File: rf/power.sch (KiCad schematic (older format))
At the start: 23 parts

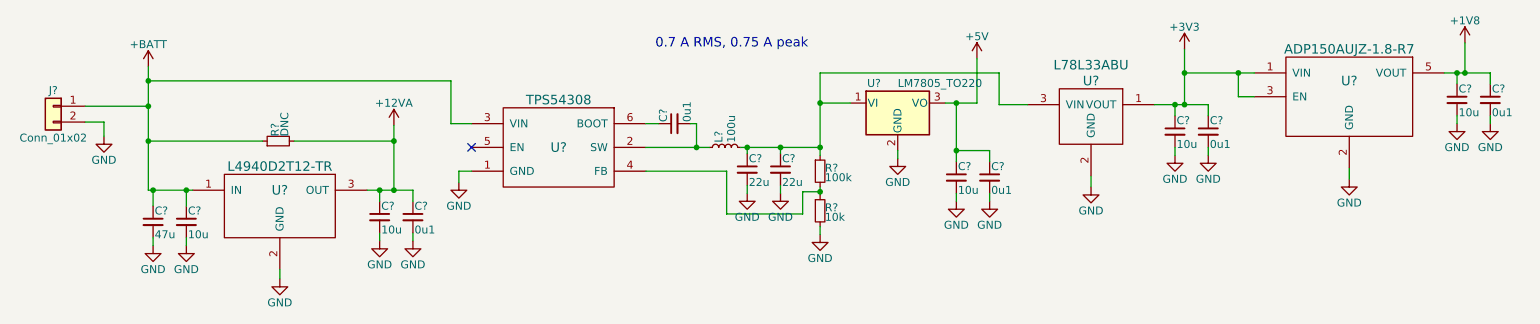
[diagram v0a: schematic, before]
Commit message: Finish assigning component footprints
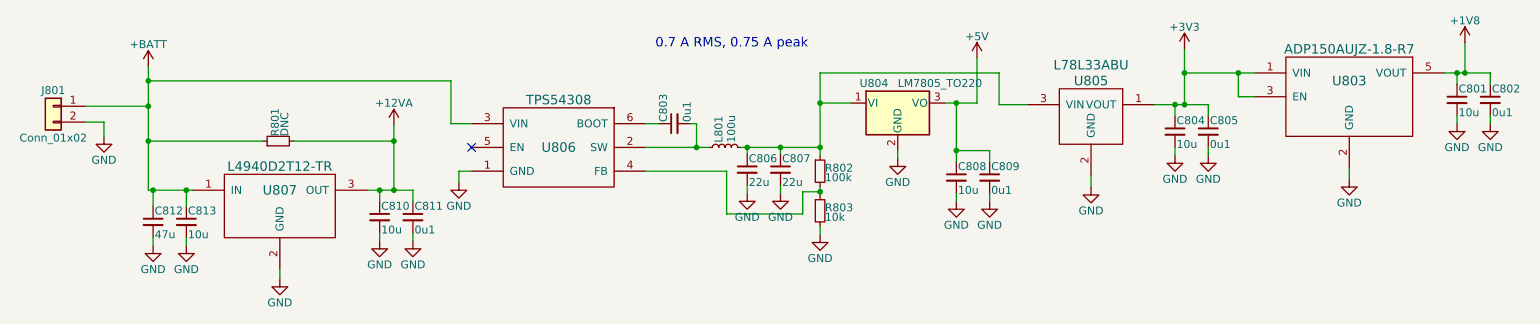
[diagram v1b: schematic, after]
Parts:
- gave numbers to parts that had none: 23

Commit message: Finish first revision layout
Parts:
- removed R801: DNC, Resistors_SMD:R_1206_HandSoldering, symbol R_Small
- removed U804: LM7805_TO220, TO_SOT_Packages_THT:TO-220_Vertical, symbol LM7805_TO220
- removed U807: L4940D2T12-TR, rajsradar:D2PAK, symbol L4940D2T12-TR
- added U802: LM340MPX-5.0/NOPB, TO_SOT_Packages_SMD:SOT-223-3_TabPin2, symbol LM340MPX-5.0/NOPB
- renumbered U803 to U801, U805 to U803, U806 to U804
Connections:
- net +BATT is gone; now on net +12VA: C812.1, C813.1, J801.1 (Pin_1), U804.3 (VIN)
- net +5V: now also U802.3 (VO)
- net GND: now also U802.2 (GND)
- net at C806.1, C807.1, L801.2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: now also U802.1 (VI)
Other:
- moved on the sheet: C810, C811
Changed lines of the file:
@@
 LIBS:mc2016k30
 LIBS:cp0402q5425entr
+LIBS:lm340-5
 EELAYER 25 0
 EELAYER END
@@
 L +12VA #PWR807
 U 1 1 5A9D8F76
-P 3295 3275
-F 0 "#PWR807" H 3295 3125 50  0001 C CNN
-F 1 "+12VA" H 3295 3415 50  0000 C CNN
-F 2 "" H 3295 3275 50  0001 C CNN
-F 3 "" H 3295 3275 50  0001 C CNN
-	1    3295 3275
+P 2305 3275
+F 0 "#PWR807" H 2305 3125 50  0001 C CNN
+F 1 "+12VA" H 2305 3415 50  0000 C CNN
+F 2 "" H 2305 3275 50  0001 C CNN
+F 3 "" H 2305 3275 50  0001 C CNN
+	1    2305 3275
 	1    0    0    -1
 $EndComp
@@
 $EndComp
 $Comp
-L R_Small R801
-U 1 1 5A9D8F94
-P 2565 3375
-F 0 "R801" H 2595 3395 50  0000 L CNN
-F 1 "DNC" H 2595 3335 50  0000 L CNN
-F 2 "Resistors_SMD:R_1206_HandSoldering" H 2565 3375 50  0001 C CNN
-F 3 "" H 2565 3375 50  0001 C CNN
-	1    2565 3375
-	0    -1   -1   0
-$EndComp
-$Comp
-L L4940D2T12-TR U807
-U 1 1 5A9D8F9B
-P 2575 3685
-F 0 "U807" H 2575 3685 60  0000 C CNN
-F 1 "L4940D2T12-TR" H 2575 3835 60  0000 C CNN
-F 2 "rajsradar:D2PAK" H 2575 3685 60  0001 C CNN
-F 3 "" H 2575 3685 60  0001 C CNN
-	1    2575 3685
-	1    0    0    -1
-$EndComp
-$Comp
-L TPS54308 U806
+L TPS54308 U804
 U 1 1 5A9D8FA2
 P 4335 3415
-F 0 "U806" H 4335 3415 60  0000 C CNN
+F 0 "U804" H 4335 3415 60  0000 C CNN
 F 1 "TPS54308" H 4335 3715 60  0000 C CNN
 F 2 "rajsradar:TI-SOT-23-6" H 4335 3415 60  0001 C CNN
@@
 NoConn ~ 3785 3415
 $Comp
-L GND #PWR824
-U 1 1 5A9D8FAA
-P 2575 4245
-F 0 "#PWR824" H 2575 3995 50  0001 C CNN
-F 1 "GND" H 2575 4095 50  0000 C CNN
-F 2 "" H 2575 4245 50  0001 C CNN
-F 3 "" H 2575 4245 50  0001 C CNN
-	1    2575 4245
-	1    0    0    -1
-$EndComp
-$Comp
-L GND #PWR813
+L GND #PWR812
 U 1 1 5A9D8FB0
 P 3705 3635
-F 0 "#PWR813" H 3705 3385 50  0001 C CNN
+F 0 "#PWR812" H 3705 3385 50  0001 C CNN
 F 1 "GND" H 3705 3485 50  0000 C CNN
 F 2 "" H 3705 3635 50  0001 C CNN
@@
 L C_Small C810
 U 1 1 5A9D8FF2
-P 3205 3855
-F 0 "C810" H 3215 3925 50  0000 L CNN
-F 1 "10u" H 3215 3775 50  0000 L CNN
-F 2 "Capacitors_SMD:C_0805_HandSoldering" H 3205 3855 50  0001 C CNN
-F 3 "" H 3205 3855 50  0001 C CNN
-	1    3205 3855
+P 2215 3855
+F 0 "C810" H 2225 3925 50  0000 L CNN
+F 1 "10u" H 2225 3775 50  0000 L CNN
+F 2 "Capacitors_SMD:C_0805_HandSoldering" H 2215 3855 50  0001 C CNN
+F 3 "" H 2215 3855 50  0001 C CNN
+	1    2215 3855
 	1    0    0    -1
 $EndComp
@@
 L C_Small C811
 U 1 1 5A9D8FF9
-P 3415 3855
-F 0 "C811" H 3425 3925 50  0000 L CNN
-F 1 "0u1" H 3425 3775 50  0000 L CNN
-F 2 "Capacitors_SMD:C_0603_HandSoldering" H 3415 3855 50  0001 C CNN
-F 3 "" H 3415 3855 50  0001 C CNN
-	1    3415 3855
+P 2425 3855
+F 0 "C811" H 2435 3925 50  0000 L CNN
+F 1 "0u1" H 2435 3775 50  0000 L CNN
+F 2 "Capacitors_SMD:C_0603_HandSoldering" H 2425 3855 50  0001 C CNN
+F 3 "" H 2425 3855 50  0001 C CNN
+	1    2425 3855
 	1    0    0    -1
 $EndComp
@@
 L GND #PWR820
 U 1 1 5A9D9000
-P 3205 4005
-F 0 "#PWR820" H 3205 3755 50  0001 C CNN
-F 1 "GND" H 3205 3855 50  0000 C CNN
-F 2 "" H 3205 4005 50  0001 C CNN
-F 3 "" H 3205 4005 50  0001 C CNN
-	1    3205 4005
+P 2215 4005
+F 0 "#PWR820" H 2215 3755 50  0001 C CNN
+F 1 "GND" H 2215 3855 50  0000 C CNN
+F 2 "" H 2215 4005 50  0001 C CNN
+F 3 "" H 2215 4005 50  0001 C CNN
+	1    2215 4005
 	1    0    0    -1
 $EndComp
@@
 L GND #PWR821
 U 1 1 5A9D9006
-P 3415 4005
-F 0 "#PWR821" H 3415 3755 50  0001 C CNN
-F 1 "GND" H 3415 3855 50  0000 C CNN
-F 2 "" H 3415 4005 50  0001 C CNN
-F 3 "" H 3415 4005 50  0001 C CNN
-	1    3415 4005
+P 2425 4005
+F 0 "#PWR821" H 2425 3755 50  0001 C CNN
+F 1 "GND" H 2425 3855 50  0000 C CNN
+F 2 "" H 2425 4005 50  0001 C CNN
+F 3 "" H 2425 4005 50  0001 C CNN
+	1    2425 4005
 	1    0    0    -1
 $EndComp
@@
 $EndComp
 $Comp
-L LM7805_TO220 U804
-U 1 1 5A9D9026
-P 6475 3135
-F 0 "U804" H 6325 3260 50  0000 C CNN
-F 1 "LM7805_TO220" H 6475 3260 50  0000 L CNN
-F 2 "TO_SOT_Packages_THT:TO-220_Vertical" H 6475 3360 50  0001 C CIN
-F 3 "" H 6475 3085 50  0001 C CNN
-	1    6475 3135
-	1    0    0    -1
-$EndComp
-$Comp
-L L78L33ABU U805
+L L78L33ABU U803
 U 1 1 5A9D902D
 P 7695 3145
-F 0 "U805" H 7695 3295 60  0000 C CNN
+F 0 "U803" H 7695 3295 60  0000 C CNN
 F 1 "L78L33ABU" H 7695 3395 60  0000 C CNN
 F 2 "TO_SOT_Packages_SMD:SOT-89-3_Handsoldering" H 7695 3145 60  0001 C CNN
@@
 $EndComp
 $Comp
-L ADP150AUJZ-1.8-R7 U803
+L ADP150AUJZ-1.8-R7 U801
 U 1 1 5A9D9034
 P 9325 2995
-F 0 "U803" H 9325 2995 60  0000 C CNN
+F 0 "U801" H 9325 2995 60  0000 C CNN
 F 1 "ADP150AUJZ-1.8-R7" H 9325 3195 60  0000 C CNN
 F 2 "rajsradar:TSOT-23" H 9325 2995 60  0001 C CNN
@@
 $EndComp
 $Comp
-L GND #PWR811
+L GND #PWR813
 U 1 1 5A9D903B
-P 6475 3485
-F 0 "#PWR811" H 6475 3235 50  0001 C CNN
-F 1 "GND" H 6475 3335 50  0000 C CNN
-F 2 "" H 6475 3485 50  0001 C CNN
-F 3 "" H 6475 3485 50  0001 C CNN
-	1    6475 3485
+P 6475 3650
+F 0 "#PWR813" H 6475 3400 50  0001 C CNN
+F 1 "GND" H 6475 3500 50  0000 C CNN
+F 2 "" H 6475 3650 50  0001 C CNN
+F 3 "" H 6475 3650 50  0001 C CNN
+	1    6475 3650
 	1    0    0    -1
 $EndComp
@@
 $EndComp
 $Comp
-L GND #PWR812
+L GND #PWR811
 U 1 1 5A9D9047
 P 9325 3615
-F 0 "#PWR812" H 9325 3365 50  0001 C CNN
+F 0 "#PWR811" H 9325 3365 50  0001 C CNN
 F 1 "GND" H 9325 3465 50  0000 C CNN
 F 2 "" H 9325 3615 50  0001 C CNN
@@
 	1745 2905 1745 3685
 Wire Wire Line
-	1745 3375 2465 3375
-Wire Wire Line
-	3295 3275 3295 3685
-Wire Wire Line
-	3295 3375 2665 3375
-Wire Wire Line
-	1745 3685 2025 3685
-Connection ~ 1745 3375
-Wire Wire Line
-	3125 3685 3415 3685
-Connection ~ 3295 3375
-Wire Wire Line
-	2575 4185 2575 4245
+	2305 3275 2305 3685
+Wire Wire Line
+	1745 3685 2425 3685
 Wire Wire Line
 	3785 3565 3705 3565
@@
 	5985 3965 5985 3915
 Wire Wire Line
-	3415 3955 3415 4005
-Wire Wire Line
-	3205 3955 3205 4005
+	2425 3955 2425 4005
+Wire Wire Line
+	2215 3955 2215 4005
 Wire Wire Line
 	1775 3985 1775 4035
@@
 Connection ~ 1775 3685
 Wire Wire Line
-	3415 3685 3415 3755
-Connection ~ 3295 3685
-Wire Wire Line
-	3205 3755 3205 3685
-Connection ~ 3205 3685
+	2425 3685 2425 3755
+Connection ~ 2305 3685
+Wire Wire Line
+	2215 3755 2215 3685
+Connection ~ 2215 3685
 Wire Wire Line
 	7295 3145 7115 3145
@@
 	7055 3435 6845 3435
 Connection ~ 6845 3435
-Wire Wire Line
-	6475 3435 6475 3485
 Wire Wire Line
 	7115 2945 5985 2945
@@
 Wire Wire Line
 	1465 3255 1345 3255
+$Comp
+L LM340MPX-5.0/NOPB U802
+U 1 1 5ACE954B
+P 6475 3135
+F 0 "U802" H 6475 3285 60  0000 C CNN
+F 1 "LM340MPX-5.0/NOPB" H 6475 3435 60  0000 C CNN
+F 2 "TO_SOT_Packages_SMD:SOT-223-3_TabPin2" H 6475 3135 60  0001 C CNN
+F 3 "" H 6475 3135 60  0001 C CNN
+	1    6475 3135
+	1    0    0    -1
+$EndComp
+Wire Wire Line
+	6475 3535 6475 3650
 $EndSCHEMATC

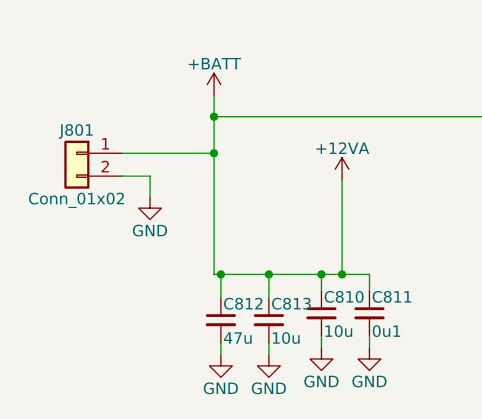
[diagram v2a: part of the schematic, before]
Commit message: Line up connectors across both boards, spread out component footprints
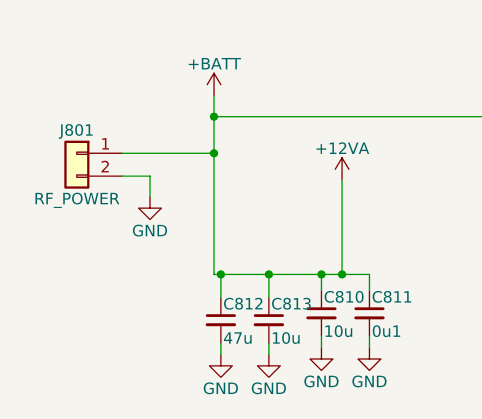
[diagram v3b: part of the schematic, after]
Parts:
- J801: value Conn_01x02 -> RF_POWER
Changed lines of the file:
@@
 P 1145 3155
 F 0 "J801" H 1145 3255 50  0000 C CNN
-F 1 "Conn_01x02" H 1145 2955 50  0000 C CNN
+F 1 "RF_POWER" H 1145 2955 50  0000 C CNN
 F 2 "Socket_Strips:Socket_Strip_Straight_1x02_Pitch2.54mm" H 1145 3155 50  0001 C CNN
 F 3 "" H 1145 3155 50  0001 C CNN
